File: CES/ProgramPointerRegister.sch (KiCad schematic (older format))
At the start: 8 parts, among them U501 RP1, U502 RP2, U503 RP3, U504 RP4

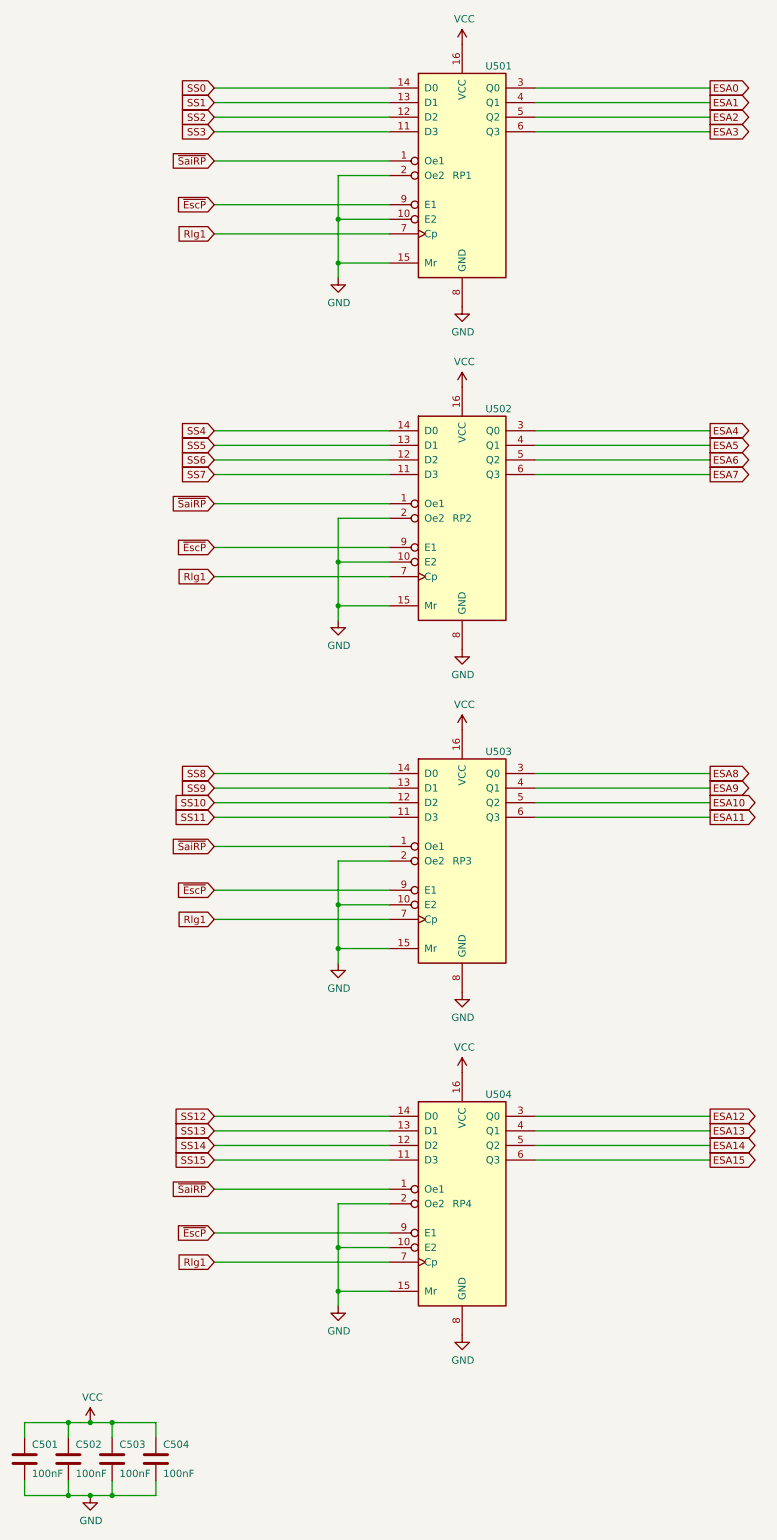
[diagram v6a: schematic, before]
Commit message: Correcting footprints errors
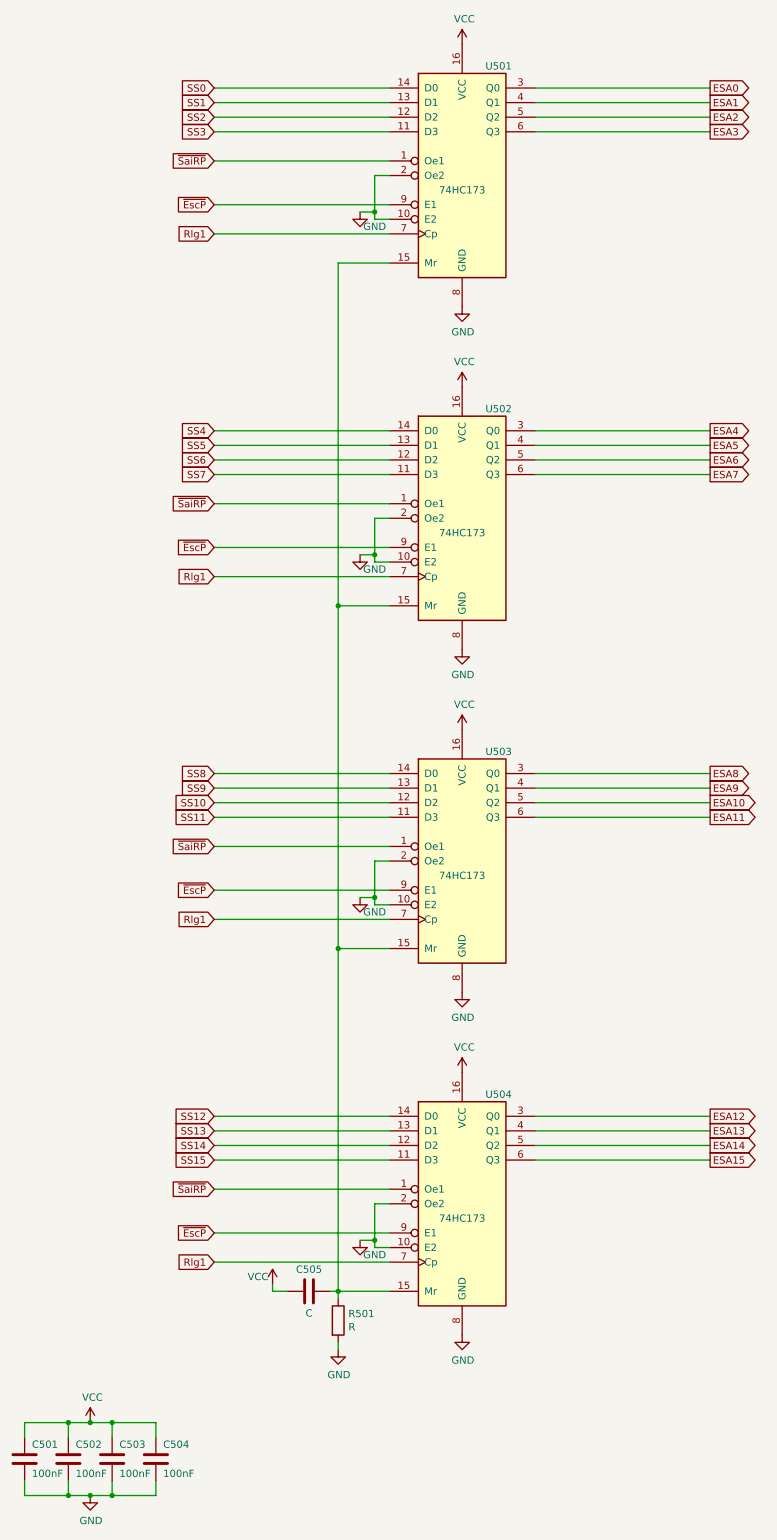
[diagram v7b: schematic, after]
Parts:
- added C505: C, Capacitor_THT:C_Disc_D4.3mm_W1.9mm_P5.00mm, symbol Device:C
- added R501: R, Resistor_THT:R_Axial_DIN0204_L3.6mm_D1.6mm_P1.90mm_Vertical, symbol Device:R
- C501, C502, C503, C504: footprint Capacitor_THT:CP_Radial_D5.0mm_P2.50mm -> Capacitor_THT:C_Disc_D4.3mm_W1.9mm_P5.00mm
- U501: value RP1 -> 74HC173
- U502: value RP2 -> 74HC173
- U503: value RP3 -> 74HC173
- U504: value RP4 -> 74HC173
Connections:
- net GND: now also R501.2; no longer U501.15 (Mr), U502.15 (Mr), U503.15 (Mr), U504.15 (Mr)
- net VCC: now also C505.1
- new net: C505.2, R501.1, U501.15 (Mr), U502.15 (Mr), U503.15 (Mr), U504.15 (Mr)
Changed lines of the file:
@@
 $EndDescr
 $Comp
-L power:VCC #PWR0507
+L power:VCC #PWR0509
 U 1 1 609BE1F2
 P 4050 800
-F 0 "#PWR0507" H 4050 650 50  0001 C CNN
+F 0 "#PWR0509" H 4050 650 50  0001 C CNN
 F 1 "VCC" H 4065 973 50  0000 C CNN
 F 2 "" H 4050 800 50  0001 C CNN
@@
 $EndComp
 $Comp
-L power:GND #PWR0508
+L power:GND #PWR0510
 U 1 1 609BEB3B
 P 4050 2600
-F 0 "#PWR0508" H 4050 2350 50  0001 C CNN
+F 0 "#PWR0510" H 4050 2350 50  0001 C CNN
 F 1 "GND" H 4055 2427 50  0000 C CNN
 F 2 "" H 4050 2600 50  0001 C CNN
@@
 $EndComp
 $Comp
-L power:VCC #PWR0509
+L power:VCC #PWR0511
 U 1 1 609BF0A7
 P 4050 3150
-F 0 "#PWR0509" H 4050 3000 50  0001 C CNN
+F 0 "#PWR0511" H 4050 3000 50  0001 C CNN
 F 1 "VCC" H 4065 3323 50  0000 C CNN
 F 2 "" H 4050 3150 50  0001 C CNN
@@
 $EndComp
 $Comp
-L power:GND #PWR0510
+L power:GND #PWR0512
 U 1 1 609C0430
 P 4050 4950
-F 0 "#PWR0510" H 4050 4700 50  0001 C CNN
+F 0 "#PWR0512" H 4050 4700 50  0001 C CNN
 F 1 "GND" H 4055 4777 50  0000 C CNN
 F 2 "" H 4050 4950 50  0001 C CNN
@@
 $EndComp
 $Comp
-L power:VCC #PWR0511
+L power:VCC #PWR0513
 U 1 1 609C13FE
 P 4050 5500
-F 0 "#PWR0511" H 4050 5350 50  0001 C CNN
+F 0 "#PWR0513" H 4050 5350 50  0001 C CNN
 F 1 "VCC" H 4065 5673 50  0000 C CNN
 F 2 "" H 4050 5500 50  0001 C CNN
@@
 $EndComp
 $Comp
-L power:VCC #PWR0513
+L power:VCC #PWR0515
 U 1 1 609C28D0
 P 4050 7850
-F 0 "#PWR0513" H 4050 7700 50  0001 C CNN
+F 0 "#PWR0515" H 4050 7700 50  0001 C CNN
 F 1 "VCC" H 4065 8023 50  0000 C CNN
 F 2 "" H 4050 7850 50  0001 C CNN
@@
 $EndComp
 $Comp
-L power:GND #PWR0512
+L power:GND #PWR0514
 U 1 1 609C2FAA
 P 4050 7300
-F 0 "#PWR0512" H 4050 7050 50  0001 C CNN
+F 0 "#PWR0514" H 4050 7050 50  0001 C CNN
 F 1 "GND" H 4055 7127 50  0000 C CNN
 F 2 "" H 4050 7300 50  0001 C CNN
@@
 $EndComp
 $Comp
-L power:GND #PWR0514
+L power:GND #PWR0516
 U 1 1 609C3E2C
 P 4050 9650
-F 0 "#PWR0514" H 4050 9400 50  0001 C CNN
+F 0 "#PWR0516" H 4050 9400 50  0001 C CNN
 F 1 "GND" H 4055 9477 50  0000 C CNN
 F 2 "" H 4050 9650 50  0001 C CNN
@@
 $EndComp
 Wire Wire Line
-	3550 1700 3200 1700
-Wire Wire Line
-	3200 1700 3200 2000
-Wire Wire Line
-	3200 2000 3550 2000
-Wire Wire Line
-	3200 2000 3200 2300
+	3550 1700 3450 1700
+Wire Wire Line
+	3450 1700 3450 1950
+Wire Wire Line
+	3450 2000 3550 2000
 Wire Wire Line
 	3200 2300 3550 2300
-Connection ~ 3200 2000
-$Comp
-L power:GND #PWR0503
+$Comp
+L power:GND #PWR0505
 U 1 1 609C59EF
-P 3200 2400
-F 0 "#PWR0503" H 3200 2150 50  0001 C CNN
-F 1 "GND" H 3205 2227 50  0000 C CNN
-F 2 "" H 3200 2400 50  0001 C CNN
-F 3 "" H 3200 2400 50  0001 C CNN
-	1    3200 2400
-	1    0    0    -1
-$EndComp
-Wire Wire Line
-	3200 2300 3200 2400
-Connection ~ 3200 2300
-Wire Wire Line
-	3550 4050 3200 4050
-Wire Wire Line
-	3200 4050 3200 4350
-Wire Wire Line
-	3200 4350 3550 4350
-Wire Wire Line
-	3200 4350 3200 4650
+P 3350 1950
+F 0 "#PWR0505" H 3350 1700 50  0001 C CNN
+F 1 "GND" H 3450 1850 50  0000 C CNN
+F 2 "" H 3350 1950 50  0001 C CNN
+F 3 "" H 3350 1950 50  0001 C CNN
+	1    3350 1950
+	1    0    0    -1
+$EndComp
+Wire Wire Line
+	3550 4050 3450 4050
+Wire Wire Line
+	3450 4050 3450 4300
+Wire Wire Line
+	3450 4350 3550 4350
 Wire Wire Line
 	3200 4650 3550 4650
-Connection ~ 3200 4350
-$Comp
-L power:GND #PWR0504
+$Comp
+L power:GND #PWR0506
 U 1 1 609C66DC
-P 3200 4750
-F 0 "#PWR0504" H 3200 4500 50  0001 C CNN
-F 1 "GND" H 3205 4577 50  0000 C CNN
-F 2 "" H 3200 4750 50  0001 C CNN
-F 3 "" H 3200 4750 50  0001 C CNN
-	1    3200 4750
-	1    0    0    -1
-$EndComp
-Wire Wire Line
-	3200 4650 3200 4750
-Connection ~ 3200 4650
-Wire Wire Line
-	3550 6400 3200 6400
-Wire Wire Line
-	3200 6400 3200 6700
-Wire Wire Line
-	3200 6700 3550 6700
-Wire Wire Line
-	3200 6700 3200 7000
+P 3350 4300
+F 0 "#PWR0506" H 3350 4050 50  0001 C CNN
+F 1 "GND" H 3450 4200 50  0000 C CNN
+F 2 "" H 3350 4300 50  0001 C CNN
+F 3 "" H 3350 4300 50  0001 C CNN
+	1    3350 4300
+	1    0    0    -1
+$EndComp
+Wire Wire Line
+	3550 6400 3450 6400
+Wire Wire Line
+	3450 6400 3450 6650
+Wire Wire Line
+	3450 6700 3550 6700
 Wire Wire Line
 	3200 7000 3550 7000
-Connection ~ 3200 6700
-$Comp
-L power:GND #PWR0505
+$Comp
+L power:GND #PWR0507
 U 1 1 609C6E61
-P 3200 7100
-F 0 "#PWR0505" H 3200 6850 50  0001 C CNN
-F 1 "GND" H 3205 6927 50  0000 C CNN
-F 2 "" H 3200 7100 50  0001 C CNN
-F 3 "" H 3200 7100 50  0001 C CNN
-	1    3200 7100
-	1    0    0    -1
-$EndComp
-Wire Wire Line
-	3200 7000 3200 7100
-Connection ~ 3200 7000
-Wire Wire Line
-	3550 8750 3200 8750
-Wire Wire Line
-	3200 8750 3200 9050
-Wire Wire Line
-	3200 9050 3550 9050
-Wire Wire Line
-	3200 9050 3200 9350
-Wire Wire Line
-	3200 9350 3550 9350
-Connection ~ 3200 9050
-$Comp
-L power:GND #PWR0506
+P 3350 6650
+F 0 "#PWR0507" H 3350 6400 50  0001 C CNN
+F 1 "GND" H 3450 6550 50  0000 C CNN
+F 2 "" H 3350 6650 50  0001 C CNN
+F 3 "" H 3350 6650 50  0001 C CNN
+	1    3350 6650
+	1    0    0    -1
+$EndComp
+Wire Wire Line
+	3550 8750 3450 8750
+Wire Wire Line
+	3450 8750 3450 9000
+Wire Wire Line
+	3450 9050 3550 9050
+$Comp
+L power:GND #PWR0508
 U 1 1 609C7550
-P 3200 9450
-F 0 "#PWR0506" H 3200 9200 50  0001 C CNN
-F 1 "GND" H 3205 9277 50  0000 C CNN
-F 2 "" H 3200 9450 50  0001 C CNN
-F 3 "" H 3200 9450 50  0001 C CNN
-	1    3200 9450
-	1    0    0    -1
-$EndComp
-Wire Wire Line
-	3200 9350 3200 9450
-Connection ~ 3200 9350
+P 3350 9000
+F 0 "#PWR0508" H 3350 8750 50  0001 C CNN
+F 1 "GND" H 3450 8900 50  0000 C CNN
+F 2 "" H 3350 9000 50  0001 C CNN
+F 3 "" H 3350 9000 50  0001 C CNN
+	1    3350 9000
+	1    0    0    -1
+$EndComp
 Text GLabel 2350 9150 0    50   Input ~ 0
 Rlg1
@@
 F 0 "C501" H 1100 10600 50  0000 L CNN
 F 1 "100nF" H 1100 10400 50  0000 L CNN
-F 2 "Capacitor_THT:CP_Radial_D5.0mm_P2.50mm" H 1088 10350 50  0001 C CNN
+F 2 "Capacitor_THT:C_Disc_D4.3mm_W1.9mm_P5.00mm" H 1088 10350 50  0001 C CNN
 F 3 "~" H 1050 10500 50  0001 C CNN
 	1    1050 10500
@@
 F 0 "C502" H 1400 10600 50  0000 L CNN
 F 1 "100nF" H 1400 10400 50  0000 L CNN
-F 2 "Capacitor_THT:CP_Radial_D5.0mm_P2.50mm" H 1388 10350 50  0001 C CNN
+F 2 "Capacitor_THT:C_Disc_D4.3mm_W1.9mm_P5.00mm" H 1388 10350 50  0001 C CNN
 F 3 "~" H 1350 10500 50  0001 C CNN
 	1    1350 10500
@@
 F 0 "C503" H 1700 10600 50  0000 L CNN
 F 1 "100nF" H 1700 10400 50  0000 L CNN
-F 2 "Capacitor_THT:CP_Radial_D5.0mm_P2.50mm" H 1688 10350 50  0001 C CNN
+F 2 "Capacitor_THT:C_Disc_D4.3mm_W1.9mm_P5.00mm" H 1688 10350 50  0001 C CNN
 F 3 "~" H 1650 10500 50  0001 C CNN
 	1    1650 10500
@@
 F 0 "C504" H 2000 10600 50  0000 L CNN
 F 1 "100nF" H 2000 10400 50  0000 L CNN
-F 2 "Capacitor_THT:CP_Radial_D5.0mm_P2.50mm" H 1988 10350 50  0001 C CNN
+F 2 "Capacitor_THT:C_Disc_D4.3mm_W1.9mm_P5.00mm" H 1988 10350 50  0001 C CNN
 F 3 "~" H 1950 10500 50  0001 C CNN
 	1    1950 10500
@@
 P 4050 1700
 F 0 "U501" H 4300 2450 50  0000 C CNN
-F 1 "RP1" H 4050 1700 50  0000 C CNN
+F 1 "74HC173" H 4050 1600 50  0000 C CNN
 F 2 "Package_DIP:DIP-16_W7.62mm" H 4050 1700 50  0001 C CNN
 F 3 "http://www.ti.com/lit/gpn/cd74HC173" H 4050 1700 50  0001 C CNN
@@
 P 4050 4050
 F 0 "U502" H 4300 4800 50  0000 C CNN
-F 1 "RP2" H 4050 4050 50  0000 C CNN
+F 1 "74HC173" H 4050 3950 50  0000 C CNN
 F 2 "Package_DIP:DIP-16_W7.62mm" H 4050 4050 50  0001 C CNN
 F 3 "http://www.ti.com/lit/gpn/cd74HC173" H 4050 4050 50  0001 C CNN
@@
 P 4050 6400
 F 0 "U503" H 4300 7150 50  0000 C CNN
-F 1 "RP3" H 4050 6400 50  0000 C CNN
+F 1 "74HC173" H 4050 6300 50  0000 C CNN
 F 2 "Package_DIP:DIP-16_W7.62mm" H 4050 6400 50  0001 C CNN
 F 3 "http://www.ti.com/lit/gpn/cd74HC173" H 4050 6400 50  0001 C CNN
@@
 P 4050 8750
 F 0 "U504" H 4300 9500 50  0000 C CNN
-F 1 "RP4" H 4050 8750 50  0000 C CNN
+F 1 "74HC173" H 4050 8650 50  0000 C CNN
 F 2 "Package_DIP:DIP-16_W7.62mm" H 4050 8750 50  0001 C CNN
 F 3 "http://www.ti.com/lit/gpn/cd74HC173" H 4050 8750 50  0001 C CNN
@@
 	1    0    0    -1
 $EndComp
+Wire Wire Line
+	3350 4300 3450 4300
+Connection ~ 3450 4300
+Wire Wire Line
+	3450 4300 3450 4350
+Wire Wire Line
+	3350 1950 3450 1950
+Connection ~ 3450 1950
+Wire Wire Line
+	3450 1950 3450 2000
+Wire Wire Line
+	3350 6650 3450 6650
+Connection ~ 3450 6650
+Wire Wire Line
+	3450 6650 3450 6700
+Wire Wire Line
+	3350 9000 3450 9000
+Connection ~ 3450 9000
+Wire Wire Line
+	3450 9000 3450 9050
+Wire Wire Line
+	3200 2300 3200 4650
+Connection ~ 3200 4650
+Wire Wire Line
+	3200 4650 3200 7000
+Connection ~ 3200 7000
+Wire Wire Line
+	3200 9350 3550 9350
+Wire Wire Line
+	3200 7000 3200 9350
+$Comp
+L Device:R R501
+U 1 1 608C1D35
+P 3200 9550
+F 0 "R501" H 3270 9596 50  0000 L CNN
+F 1 "R" H 3270 9505 50  0000 L CNN
+F 2 "Resistor_THT:R_Axial_DIN0204_L3.6mm_D1.6mm_P1.90mm_Vertical" V 3130 9550 50  0001 C CNN
+F 3 "~" H 3200 9550 50  0001 C CNN
+	1    3200 9550
+	1    0    0    -1
+$EndComp
+$Comp
+L Device:C C505
+U 1 1 608C2792
+P 3000 9350
+F 0 "C505" V 3150 9350 50  0000 C CNN
+F 1 "C" V 2850 9350 50  0000 C CNN
+F 2 "Capacitor_THT:C_Disc_D4.3mm_W1.9mm_P5.00mm" H 3038 9200 50  0001 C CNN
+F 3 "~" H 3000 9350 50  0001 C CNN
+	1    3000 9350
+	0    -1   -1   0
+$EndComp
+$Comp
+L power:VCC #PWR0503
+U 1 1 608C3296
+P 2750 9300
+F 0 "#PWR0503" H 2750 9150 50  0001 C CNN
+F 1 "VCC" H 2650 9350 50  0000 C CNN
+F 2 "" H 2750 9300 50  0001 C CNN
+F 3 "" H 2750 9300 50  0001 C CNN
+	1    2750 9300
+	1    0    0    -1
+$EndComp
+$Comp
+L power:GND #PWR0504
+U 1 1 608C3AA6
+P 3200 9750
+F 0 "#PWR0504" H 3200 9500 50  0001 C CNN
+F 1 "GND" H 3205 9577 50  0000 C CNN
+F 2 "" H 3200 9750 50  0001 C CNN
+F 3 "" H 3200 9750 50  0001 C CNN
+	1    3200 9750
+	1    0    0    -1
+$EndComp
+Wire Wire Line
+	3200 9700 3200 9750
+Wire Wire Line
+	3200 9400 3200 9350
+Connection ~ 3200 9350
+Wire Wire Line
+	3150 9350 3200 9350
+Wire Wire Line
+	2850 9350 2750 9350
+Wire Wire Line
+	2750 9350 2750 9300
 $EndSCHEMATC
